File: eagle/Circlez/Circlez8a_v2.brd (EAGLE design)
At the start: 46 x 46 mm, 61 parts, among them IC1 MEGA8-AI, J1 AVR_SPI_PRG_6PTH

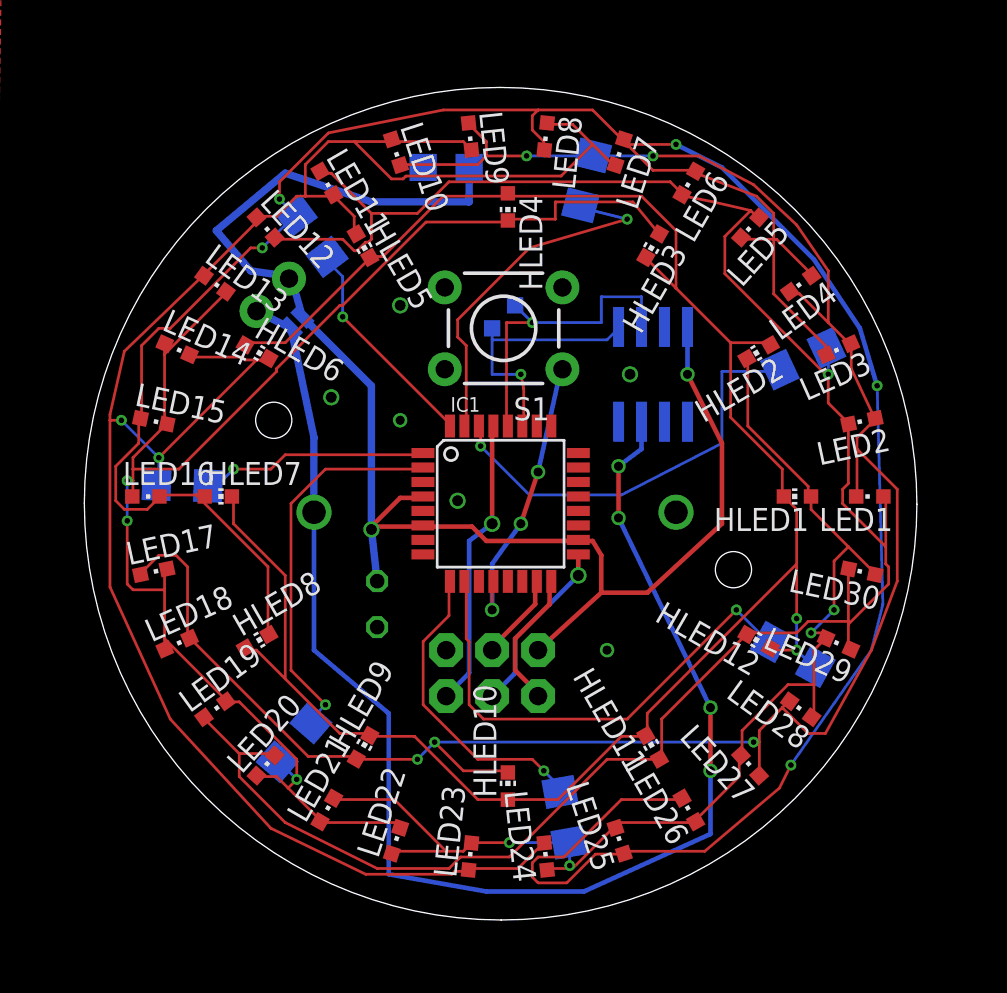
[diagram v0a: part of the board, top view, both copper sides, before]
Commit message: New version with wires farther from the border, ready for prod.
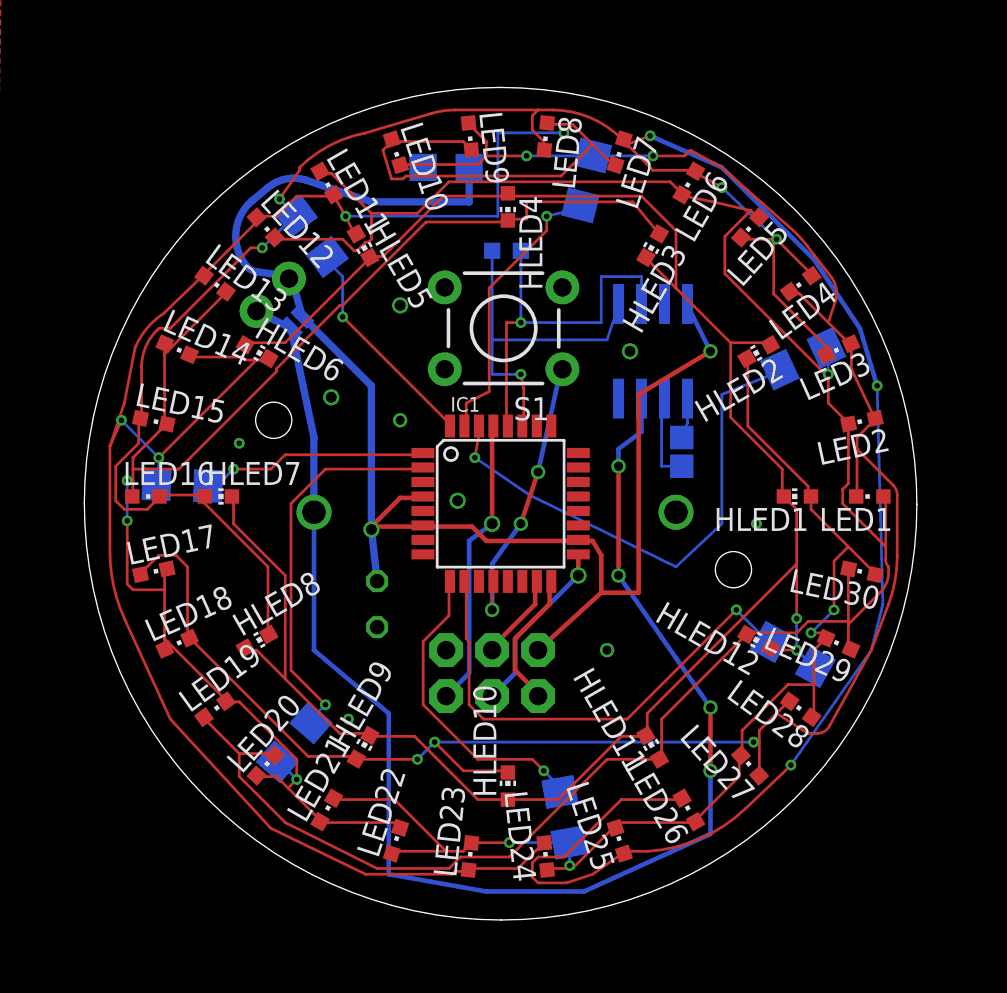
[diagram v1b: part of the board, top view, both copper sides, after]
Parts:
- added TP1, TP2: TPTP13SQ, testpad:TP13SQ
- moved TP_SDA 4.29 mm to (24.1, 38.6)
- moved TP_SCL 3.03 mm to (25.7, 38.6)
- moved U$2 1.27 mm to (33.0, 33.0)
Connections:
- new net N$22: TP1.TP, U$2.1
- new net N$23: TP2.TP, U$2.2
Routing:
- net N$10: track 112.6 -> 122.7 mm, vias 2 -> 4
- net N$24: track 14.3 -> 19.7 mm
- net N$15: track 23.6 -> 28.7 mm
- net N$23: track 0.00 -> 4.96 mm
- net N$16: track 20.1 -> 15.8 mm
- net N$12: track 17.7 -> 21.3 mm
- net N$9: track 156.1 -> 153.8 mm, vias 5 -> 7
- net N$22: track 0.00 -> 2.12 mm
- net VBAT: track 77.6 -> 79.1 mm
- net VCC: track 84.3 -> 83.5 mm
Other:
- board text added: "Circlez v2.0"
- board text added: "Crystal 32kHz"
- board text added: "March2014"
- board text added: "PB0"
- board text removed: "ADC6"
- board text removed: "ADC7"
- board text removed: "Circlez - v2.0 March2014"

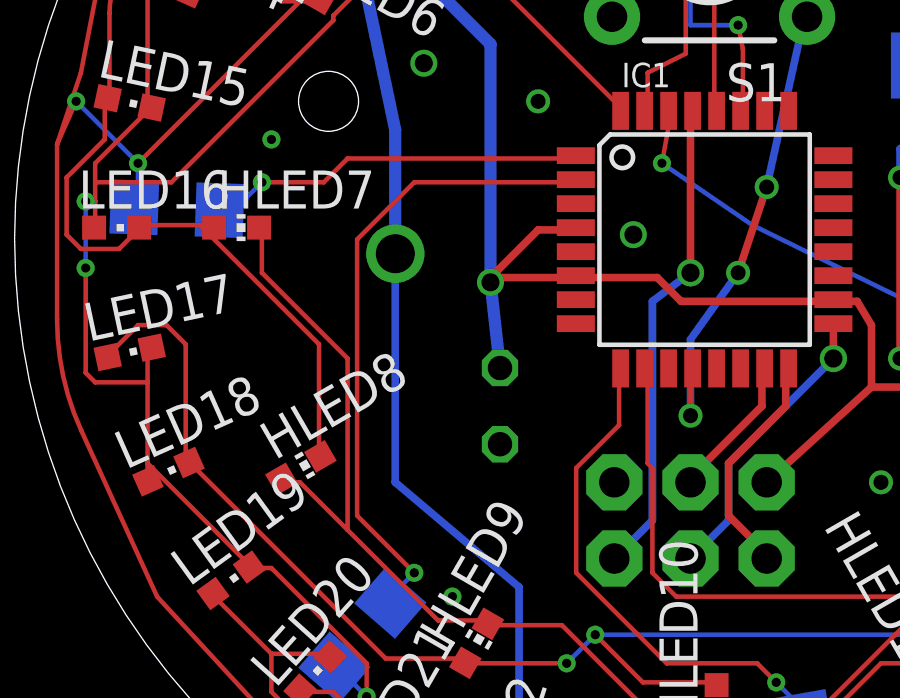
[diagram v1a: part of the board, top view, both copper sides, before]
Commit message: Minor fix in case I make another batch: one wire is too close to the VCC and careless soldering can short the pin to VCC (leds always up)
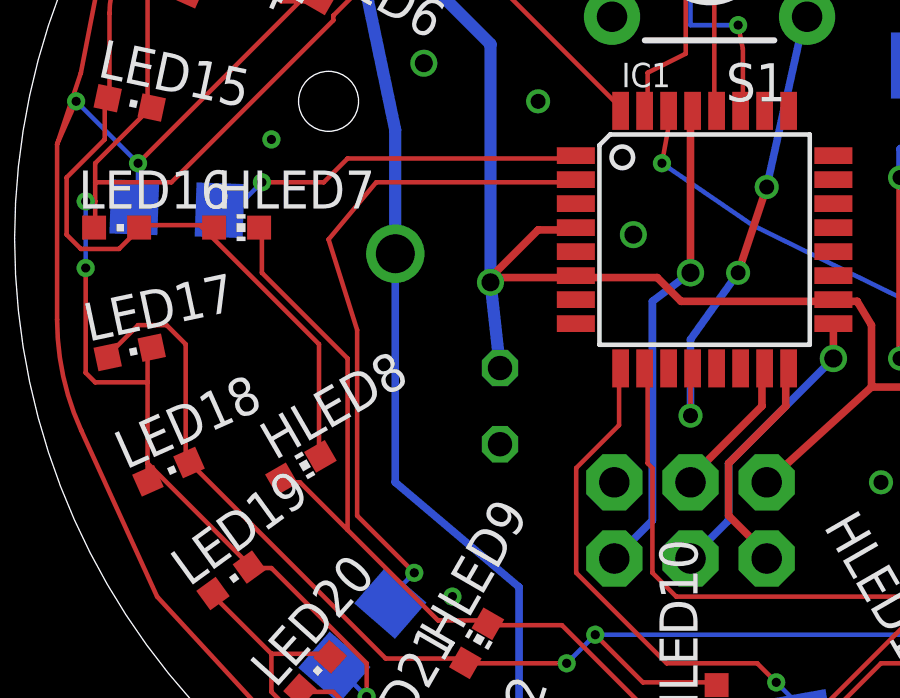
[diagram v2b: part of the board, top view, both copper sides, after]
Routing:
- net N$19: track 21.5 -> 22.7 mm
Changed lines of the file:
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@@
 <contactref element="IC1" pad="2"/>
 <contactref element="R5" pad="1"/>
-<wire x1="14.9225" y1="26.51125" x2="20.16125" y2="26.51125" width="0.1524" layer="1"/>
-<wire x1="13.0175" y1="24.60625" x2="14.9225" y2="26.51125" width="0.1524" layer="1"/>
-<wire x1="13.0175" y1="15.39875" x2="13.0175" y2="24.60625" width="0.1524" layer="1"/>
+<wire x1="13.6525" y1="26.51125" x2="20.16125" y2="26.51125" width="0.1524" layer="1"/>
+<wire x1="12.065" y1="24.60625" x2="13.6525" y2="26.51125" width="0.1524" layer="1"/>
+<wire x1="13.0175" y1="15.39875" x2="13.0175" y2="21.59" width="0.1524" layer="1"/>
+<wire x1="13.0175" y1="21.59" x2="12.065" y2="24.60625" width="0.1524" layer="1"/>
 <wire x1="14.9225" y1="13.49375" x2="13.0175" y2="15.39875" width="0.1524" layer="1"/>
 <wire x1="13.97" y1="12.54125" x2="14.9225" y2="13.49375" width="0.1524" layer="16"/>

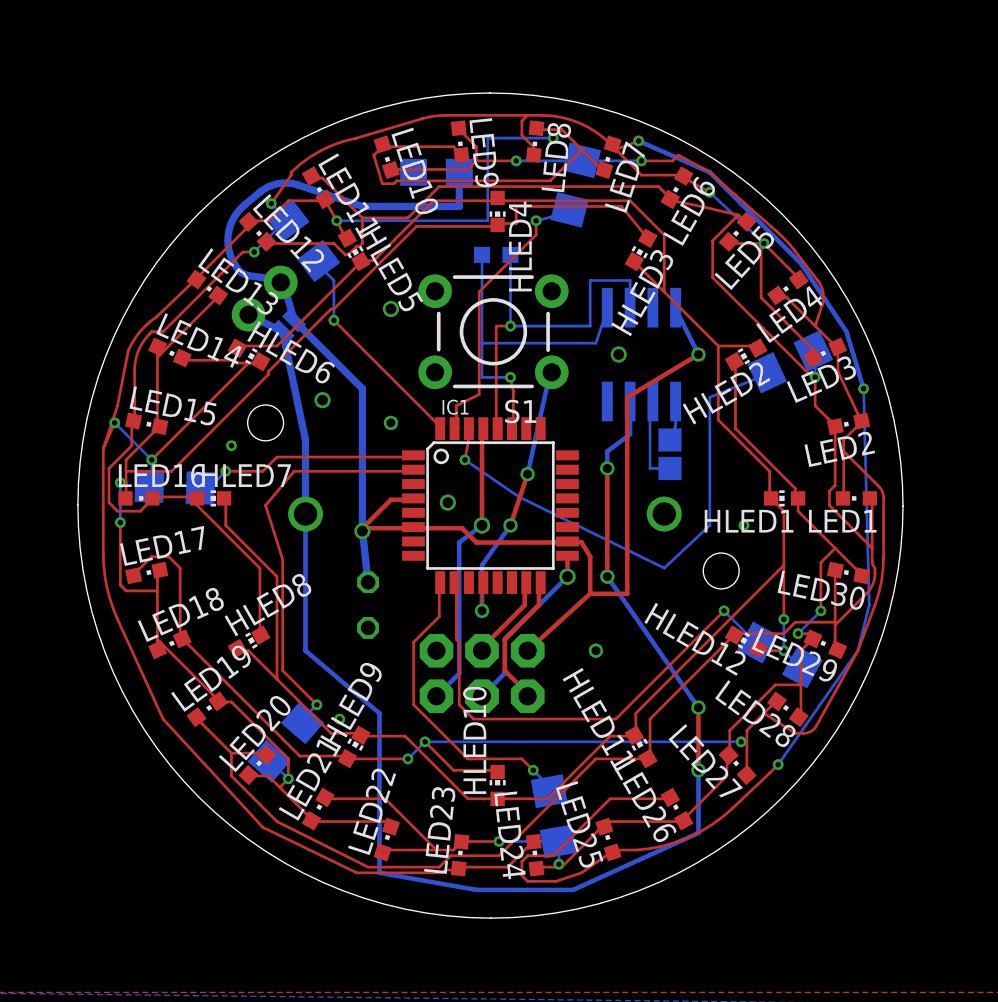
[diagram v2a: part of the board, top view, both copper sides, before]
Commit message: More space between SMD leds and surrounding traces to avoid shortcuts
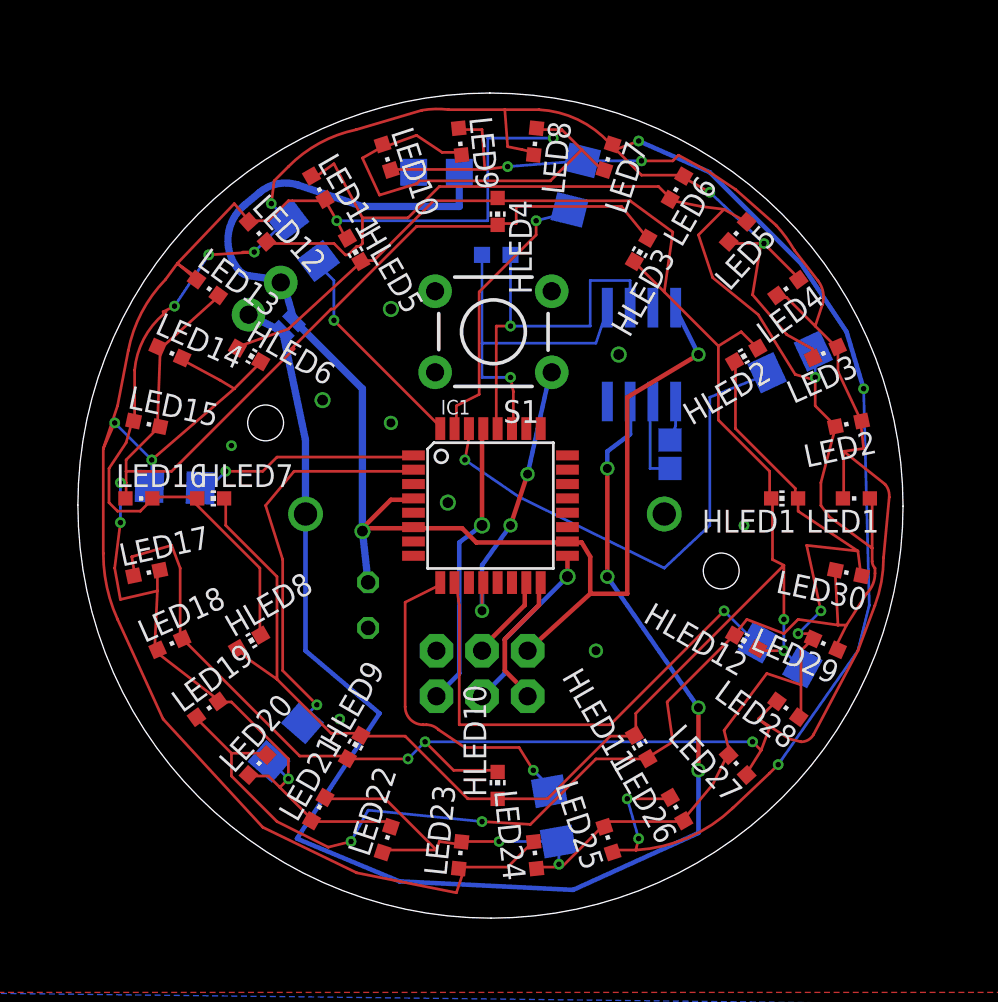
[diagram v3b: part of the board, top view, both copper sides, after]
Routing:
- net N$27: track 153.8 -> 146.4 mm, vias 7 -> 11
- net N$10: track 122.7 -> 130.0 mm
- net N$8: track 117.4 -> 123.0 mm
- net VBAT: track 79.1 -> 83.6 mm
- net N$13: track 65.6 -> 69.8 mm
- net N$2: track 119.4 -> 122.8 mm, vias 1 -> 3
- net N$20: track 17.1 -> 18.3 mm
- net N$21: track 27.1 -> 28.0 mm
- net N$11: track 86.2 -> 87.0 mm
- net N$14: track 113.0 -> 113.7 mm
